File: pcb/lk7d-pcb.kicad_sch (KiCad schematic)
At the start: 27 parts, among them J1 PINHD_1x4_Male, J2 PINHD_1x4_Male, SW1 RotaryEncoder_Switch_MP, SW2 RotaryEncoder_Switch_MP, SW3 SW_Push, SW4 SW_Push, SW5 SW_Push, SW6 SW_Push, SW7 SW_Push, SW8 SW_Push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

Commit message: Export
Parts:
- LED1, LED2, LED3, LED4, LED5, LED6: JLC (none) -> SMD; LCSC (none) -> C5149201
- SW3, SW4, SW5, SW6, SW7, SW8: JLC D2LS -> SMD; LCSC C3823622 -> C2803348
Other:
- moved on the sheet: C1, C2, D1, D2, D3, D4, D5, D6, D7, D8, J1, J2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

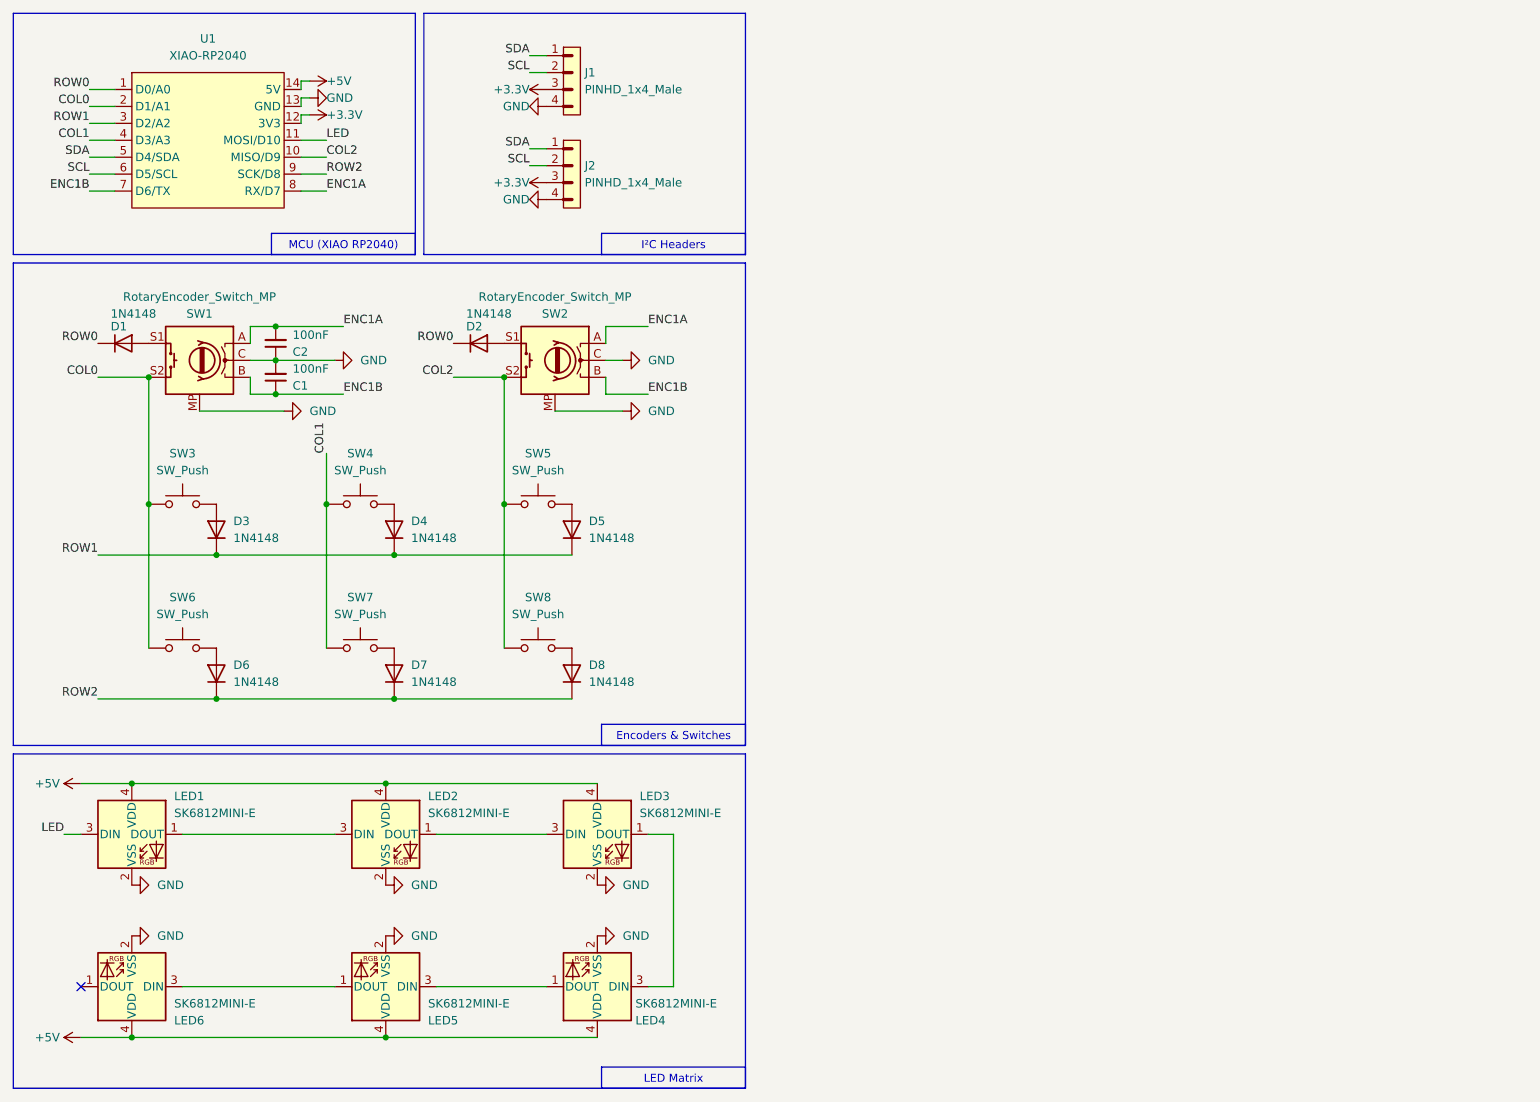
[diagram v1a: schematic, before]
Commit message: Add Logic Level Converter for per key LEDs (#3)
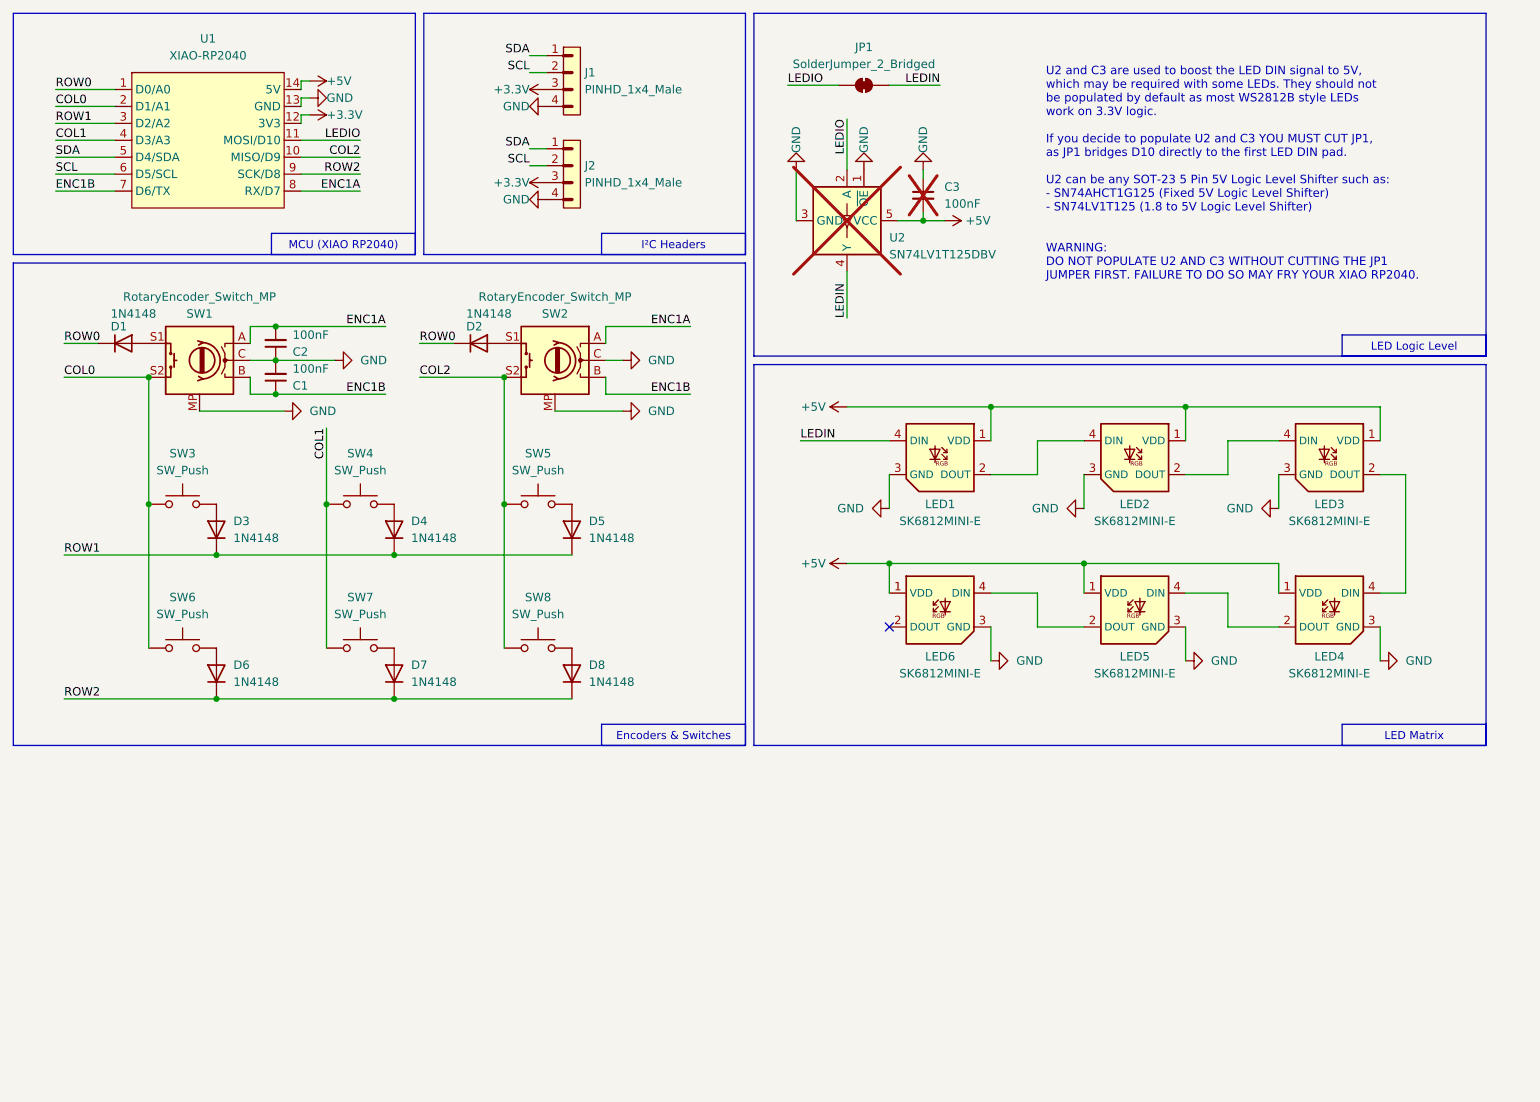
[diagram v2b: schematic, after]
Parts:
- removed LED1, LED2, LED3, LED4, LED5, LED6: SK6812MINI-E, LKBD_Common:LED_SK6812MINI-E, symbol LED:SK6812MINI
- added C3: 100nF, Capacitor_SMD:C_1206_3216Metric_Pad1.33x1.80mm_HandSolder, symbol Device:C_Small
- added JP1: SolderJumper_2_Bridged, Jumper:SolderJumper-2_P1.3mm_Bridged_RoundedPad1.0x1.5mm, symbol Jumper:SolderJumper_2_Bridged
- added LED1, LED2, LED3, LED4, LED5, LED6: SK6812MINI-E, LKBD_Common:LED_SK6812MINI-E, symbol LKBD_LED:SK6812MINI-E
- added U2: SN74LV1T125DBV, Package_TO_SOT_SMD:SOT-23-5, symbol Logic_LevelTranslator:SN74LV1T125DBV
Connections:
- net +5V: now also C3.2, LED1.1 (VDD), LED2.1 (VDD), LED3.1 (VDD), LED4.1 (VDD), LED5.1 (VDD), LED6.1 (VDD), U2.5 (VCC)
- net GND: now also C3.1, LED1.3 (GND), LED2.3 (GND), LED3.3 (GND), LED4.3 (GND), LED5.3 (GND), LED6.3 (GND), U2.1 (~{OE}), U2.3 (GND)
- net LED renamed LEDIO
- net LEDIO: now also JP1.1 (A), U2.2 (A)
- new net: LED3.2 (DOUT), LED4.4 (DIN)
- new net: LED2.2 (DOUT), LED3.4 (DIN)
- new net: LED5.2 (DOUT), LED6.4 (DIN)
- new net: LED4.2 (DOUT), LED5.4 (DIN)
- new net: LED1.2 (DOUT), LED2.4 (DIN)
- new net LEDIN: JP1.2 (B), LED1.4 (DIN), U2.4 (Y)
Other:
- note added: "LED Logic Level"
- note added: "U2 and C3 are used to boost the LED DIN signal to 5V, which may be required with some LEDs. They should not be populated by default as most WS2812B style LEDs work on 3.3V logic. If you decide to populate U2 and C3 YOU MUST CUT JP1, as JP1 bridges D10 directly to the first LED DIN pad. U2 can be any SOT-23 5 Pin 5V Logic Level Shifter such as: - SN74AHCT1G125 (Fixed 5V Logic Level Shifter) - SN74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"

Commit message: Add plate and cleanup PCB (#4)
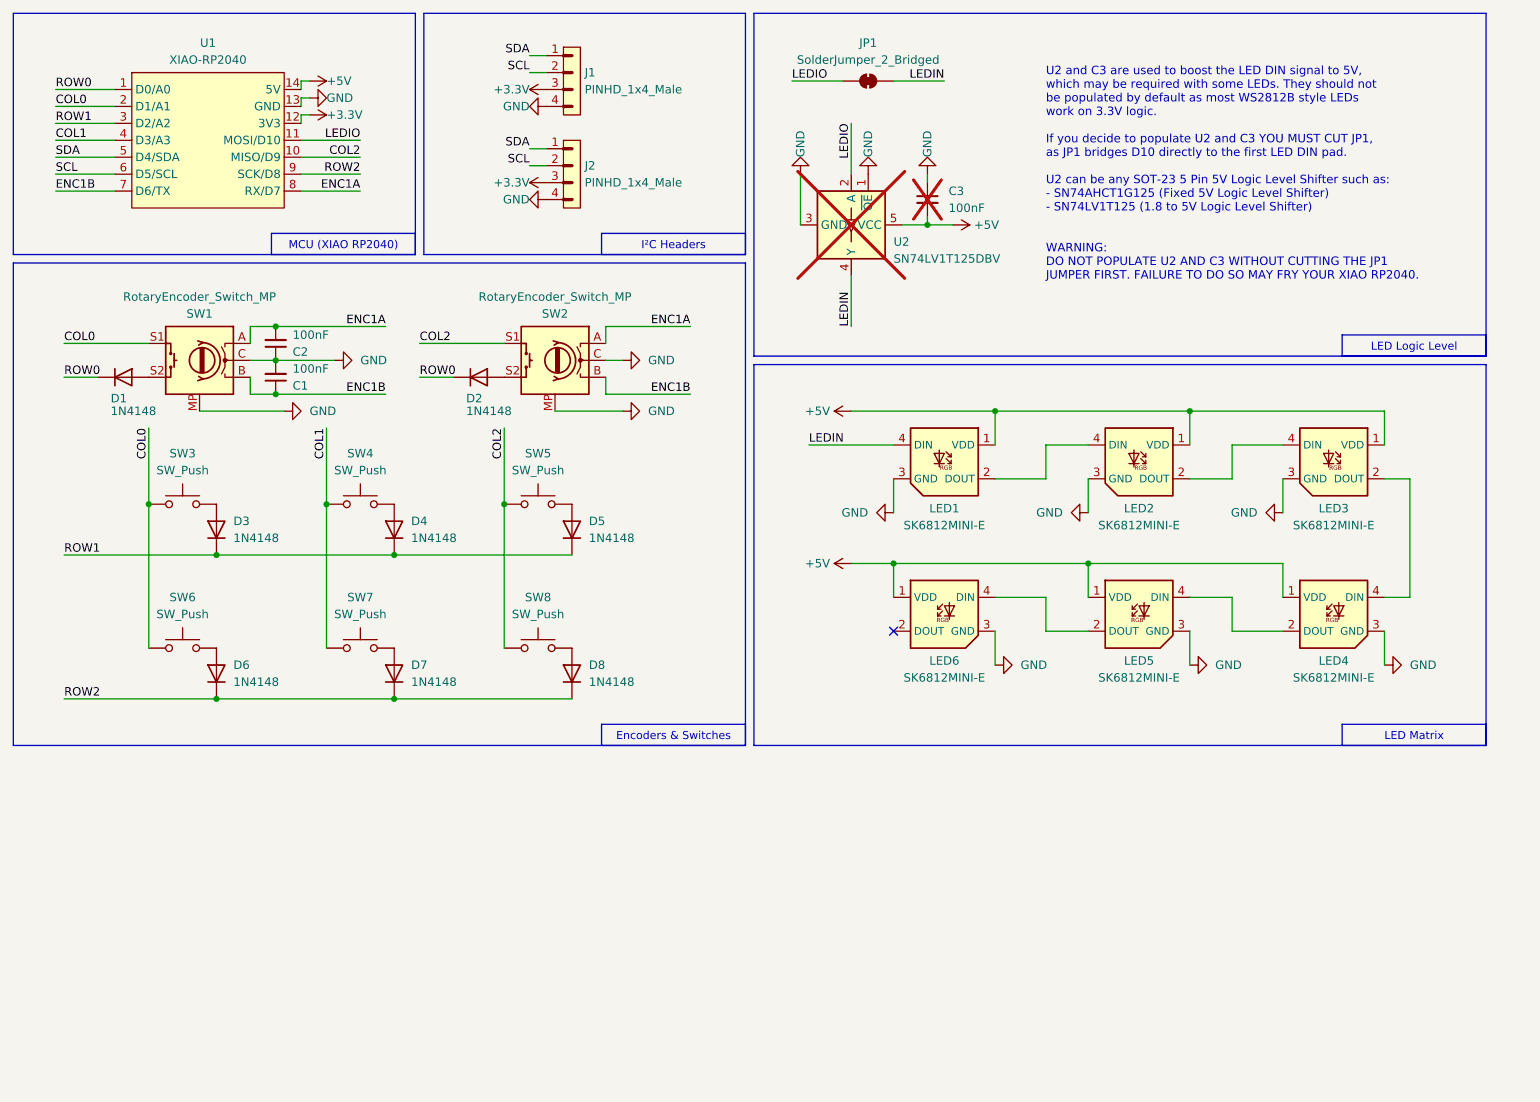
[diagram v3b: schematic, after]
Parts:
- C1, C2: footprint Capacitor_SMD:C_1206_3216Metric_Pad1.33x1.80mm_HandSolder -> LKBD_Common:Capacitor_SMD_1206_inSilk
- C3: footprint Capacitor_SMD:C_1206_3216Metric_Pad1.33x1.80mm_HandSolder -> LKBD_Common:Capacitor_SMD_1206_inSilk; JLC (none) -> 1206; LCSC (none) -> C24497
- D1, D2, D3, D4, D5, D6, D7, D8: footprint Diode_SMD:D_SOD-123 -> LKBD_Common:Diode_SMD_SOD-123_inSilk; JLCRotOffset (none) -> 180
- LED1, LED2, LED3, LED4, LED5, LED6: JLC (none) -> SMD; JLCRotOffset (none) -> 180; LCSC (none) -> C5149201
- U1: Documentation (none) -> https://wiki.seeedstudio.com/XIAO-RP2040/; JLC (none) -> SMD-14P; LCSC (none) -> C9900177322; Pinout (none) -> https://files.seeedstudio.com/wiki/XIAO-RP2040/img/xinpin.j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
- U2: JLC (none) -> SOT-23-5; LCSC (none) -> C7484
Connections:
- net COL0: now also SW1.S1; no longer SW1.S2
- net COL2: now also SW2.S1; no longer SW2.S2
- net at D1.2 (A): now also SW1.S2; no longer SW1.S1
- net at D2.2 (A): now also SW2.S2; no longer SW2.S1
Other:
- moved on the sheet: C3, D1, D2, JP1, LED1, LED2, LED3, LED4, LED5, LED6, U2

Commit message: Update LKBD libraries
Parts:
- SW1, SW2: footprint LKBD_KeySwitch:EC11_THT_sqSilk -> LKBD_KeySwitch:ROT_EC11_THT_sqSilk
- U1: footprint LKBD_MCU:MCU_XIAO-RP2040 -> LKBD_MCU:MCU_XIAO_RP2040
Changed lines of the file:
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@@
 			)
 		)
-		(property "Footprint" "LKBD_KeySwitch:EC11_THT_sqSilk"
+		(property "Footprint" "LKBD_KeySwitch:ROT_EC11_THT_sqSilk"
 			(at 99.06 61.976 0)
 			(effects
@@
 			)
 		)
-		(property "Footprint" "LKBD_MCU:MCU_XIAO-RP2040"
+		(property "Footprint" "LKBD_MCU:MCU_XIAO_RP2040"
 			(at 43.434 50.292 0)
 			(effects
@@
 			)
 		)
-		(property "Footprint" "LKBD_KeySwitch:EC11_THT_sqSilk"
+		(property "Footprint" "LKBD_KeySwitch:ROT_EC11_THT_sqSilk"
 			(at 45.72 61.976 0)
 			(effects
